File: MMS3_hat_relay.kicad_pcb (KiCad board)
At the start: 2 copper layers, 100 x 50 mm, 85 parts, among them J1 Chainbus in, J10 Conn_01x03_Pin, J2 Chainbus Out, J3 Conn_01x04_Pin, J5 Program, J6 Conn_01x03_Pin, J7 Conn_01x03_Pin, J8 Conn_01x03_Pin, J9 Conn_01x03_Pin, Q12 MMBT5551 200-300, Q13 MMBT5551 200-300, Q14 MMBT5551 200-300, Q15 MMBT5551 200-300, Q16 MMBT5551 200-300, U1 SN74CB3Q3384APW, U2 M24C64, U3 CH32V003FxPx, U4 AMS1117, U5 LTV-217-B-G, U6 LTV-217-B-G, U7 LTV-217-B-G, U8 LTV-217-B-G, U9 LTV-217-B-G, X1 X322525MOB4SI

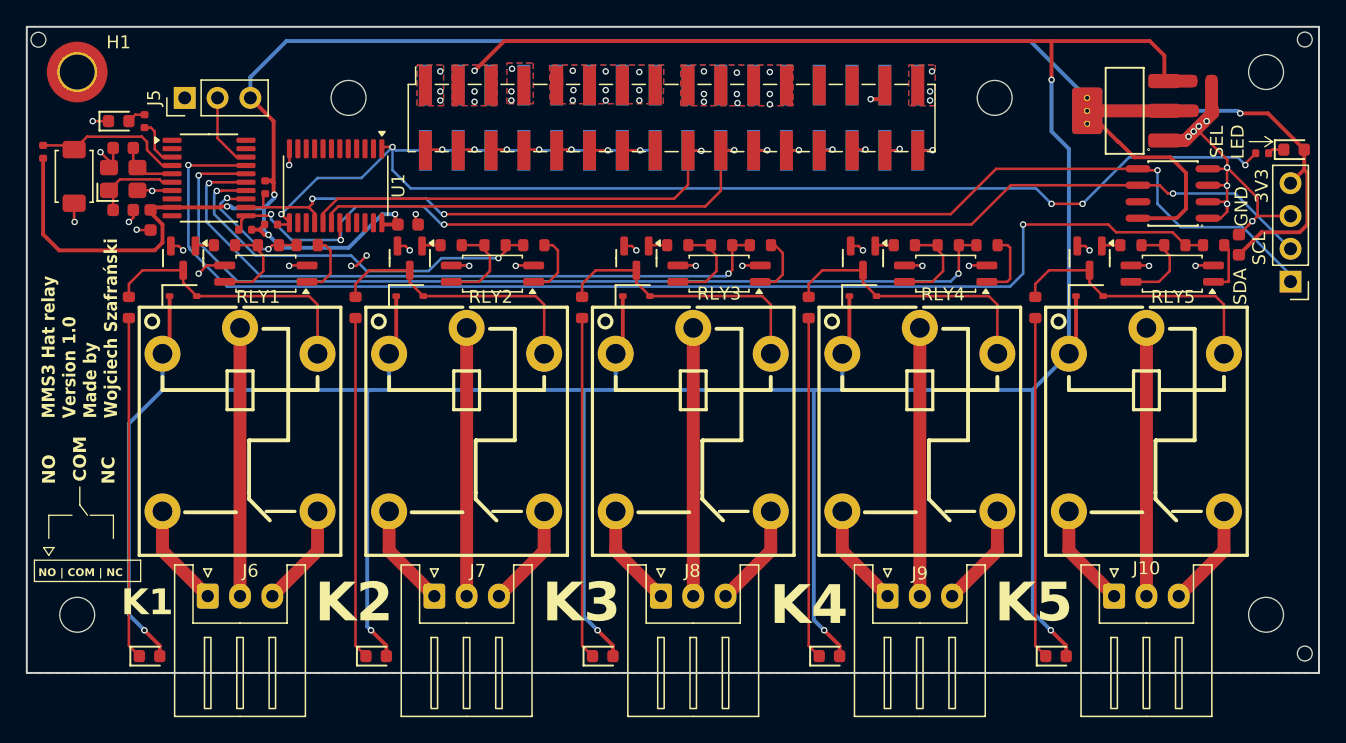
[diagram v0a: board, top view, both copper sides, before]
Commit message: fixed NPN configuration in optocoupler
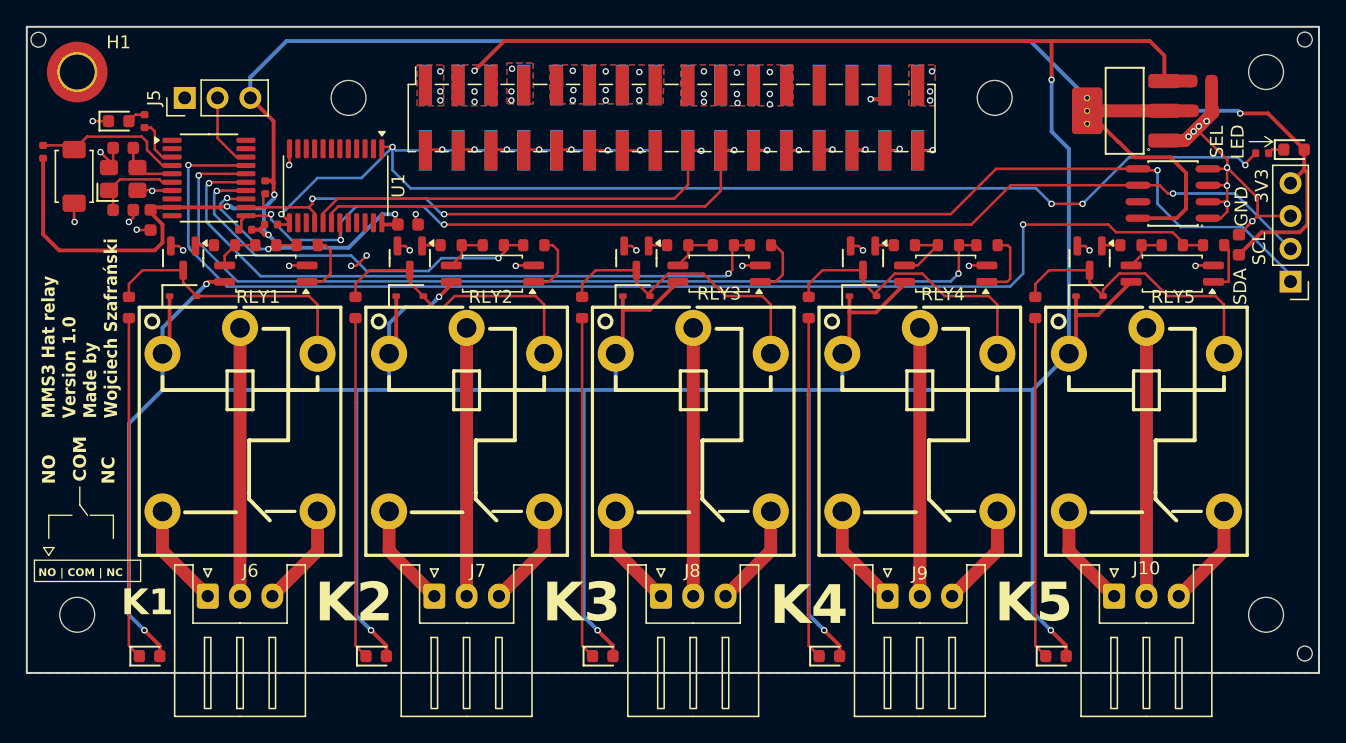
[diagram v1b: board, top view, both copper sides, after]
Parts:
- moved R15 0.20 mm to (96.6, 105.4)
- moved R28 0.20 mm to (166.7, 105.4)
- moved R19 0.14 mm to (114.2, 105.4)
- moved R22 0.13 mm to (132.0, 105.4)
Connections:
- U5 pad 3: GND -> Net-(R15-Pad2)
- U5 pad 4: Net-(R15-Pad2) -> +5V
- U6 pad 3: GND -> Net-(R19-Pad2)
- U6 pad 4: Net-(R19-Pad2) -> +5V
- U7 pad 3: GND -> Net-(R22-Pad2)
- U7 pad 4: Net-(R22-Pad2) -> +5V
- U8 pad 3: GND -> Net-(R25-Pad2)
- U8 pad 4: Net-(R25-Pad2) -> +5V
- U9 pad 3: GND -> Net-(R28-Pad2)
- U9 pad 4: Net-(R28-Pad2) -> +5V
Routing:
- net +5V: track 298.1 -> 331.3 mm, vias 9 -> 11
- net GND: track 66.2 -> 58.3 mm, vias 51 -> 46
- net Net-(R28-Pad2): track 7.04 -> 3.46 mm
- net Net-(R15-Pad2): track 7.04 -> 3.46 mm
- net Net-(R19-Pad2): track 7.04 -> 3.52 mm
- net Net-(R22-Pad2): track 7.04 -> 3.79 mm
- net Net-(R25-Pad2): track 7.04 -> 5.00 mm
- net Net-(Q16-C): track 21.5 -> 23.2 mm
- net Net-(Q15-C): track 21.5 -> 23.1 mm
- net Net-(Q14-C): track 21.5 -> 23.1 mm
- net Net-(Q13-C): track 21.5 -> 22.2 mm

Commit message: changed headers and relays to better one
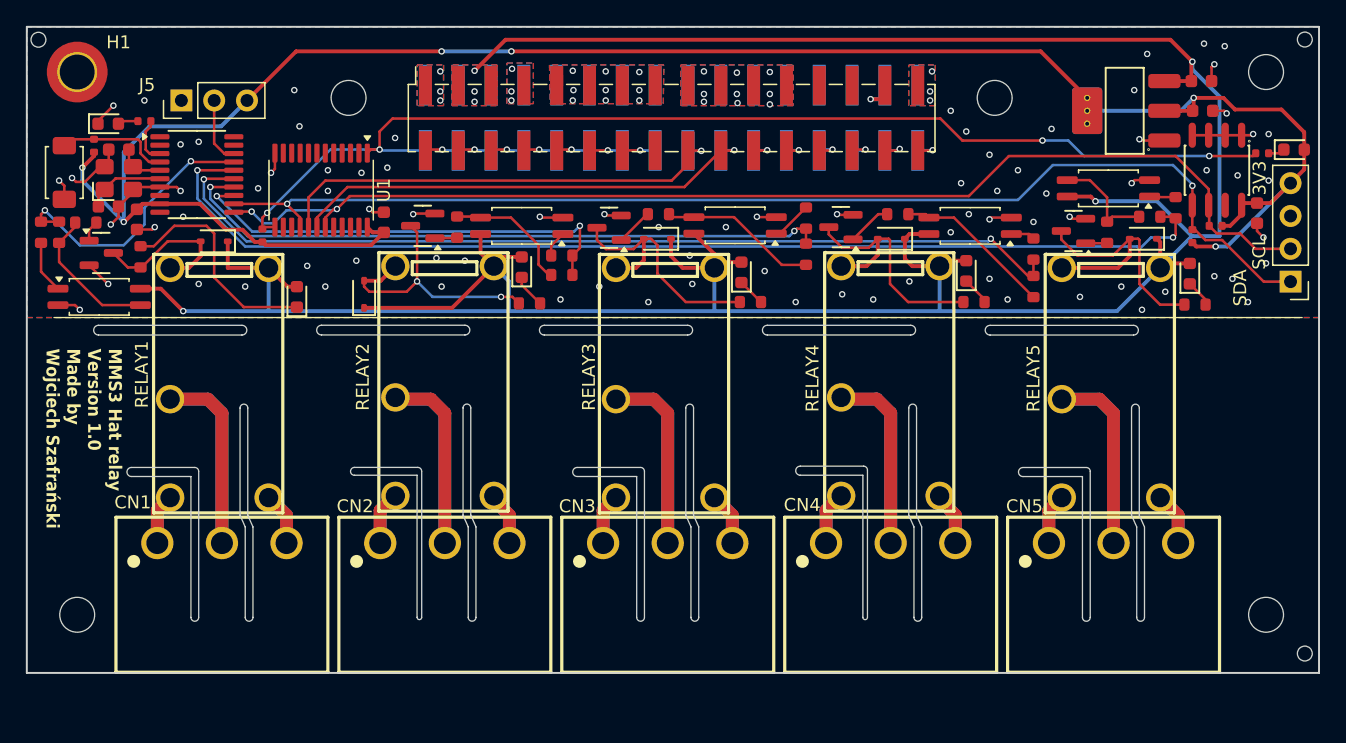
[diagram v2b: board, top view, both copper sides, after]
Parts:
- removed J10, J6, J7, J8, J9: Conn_01x03_Pin, Connector_JST:JST_XH_S3B-XH-A_1x03_P2.50mm_Horizontal
- removed RLY1, RLY2, RLY3, RLY4, RLY5: SRD-05VDC-SL-C, SRD-05VDC-SL-C:RELAY-TH_SRD-XXVDC-XL-C
- added CN1: DB2ERC-5.0-3P-GN, DB2ERC-5:CONN-TH_3P-P5.00_DB2ERC-5.0-3P-GN, F.Cu at (93.2, 128.4)
- added CN2: DB2ERC-5.0-3P-GN, DB2ERC-5:CONN-TH_3P-P5.00_DB2ERC-5.0-3P-GN, F.Cu at (110.5, 128.4)
- added CN3: DB2ERC-5.0-3P-GN, DB2ERC-5:CONN-TH_3P-P5.00_DB2ERC-5.0-3P-GN, F.Cu at (127.7, 128.4)
- added CN4: DB2ERC-5.0-3P-GN, DB2ERC-5:CONN-TH_3P-P5.00_DB2ERC-5.0-3P-GN, F.Cu at (144.9, 128.4)
- added CN5: DB2ERC-5.0-3P-GN, DB2ERC-5:CONN-TH_3P-P5.00_DB2ERC-5.0-3P-GN, F.Cu at (162.2, 128.4)
- added RELAY1: JE-105D_C3250129, JE-105D_C3250129:RELAY-TH_JE-1XXD, F.Cu at (93.0, 116.0)
- added RELAY2: JE-105D_C3250129, JE-105D_C3250129:RELAY-TH_JE-1XXD, F.Cu at (110.4, 115.9)
- added RELAY3: JE-105D_C3250129, JE-105D_C3250129:RELAY-TH_JE-1XXD, F.Cu at (127.5, 116.0)
- added RELAY4: JE-105D_C3250129, JE-105D_C3250129:RELAY-TH_JE-1XXD, F.Cu at (144.9, 115.9)
- added RELAY5: JE-105D_C3250129, JE-105D_C3250129:RELAY-TH_JE-1XXD, F.Cu at (162.0, 116.0)
- moved R6 75.1 mm to (170.1, 103.9)
- moved R10 71.8 mm to (168.3, 104.7), turned to 90 degrees
- moved D10 32.1 mm to (116.4, 107.1), turned to 90 degrees
- moved D12 31.6 mm to (150.8, 107.4), turned to 90 degrees
- moved D11 31.6 mm to (133.4, 107.5), turned to 90 degrees
- moved D13 31.4 mm to (168.1, 107.6), turned to 90 degrees
- moved D9 30.0 mm to (99.0, 109.4), turned to 90 degrees
- moved R17 20.6 mm to (79.2, 104.4), turned to -90 degrees
- moved R15 16.0 mm to (80.6, 104.4), turned to -90 degrees
- moved R31 13.5 mm to (117.0, 109.9), turned to 0 degrees
- moved R32 13.0 mm to (134.1, 109.8), turned to 0 degrees
- moved U5 13.0 mm to (83.7, 109.4), turned to 0 degrees
- moved R33 12.8 mm to (151.4, 109.8), turned to 0 degrees
- moved R34 12.4 mm to (168.5, 110.0), turned to 0 degrees
- moved R16 10.9 mm to (82.7, 103.7), turned to 0 degrees
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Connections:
- U3 pad 13: /S1 -> /S2
- U3 pad 14: /S2 -> /S3
- U3 pad 15: /S3 -> /S4
- U3 pad 16: /S4 -> /S5
- U3 pad 17: /S5 -> /S1
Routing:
- net +5V: track 331.3 -> 235.9 mm, vias 11 -> 6
- net Net-(D13-Pad1): track 26.5 -> 2.12 mm
- net Net-(D11-Pad1): track 26.5 -> 2.15 mm
- net Net-(D12-Pad1): track 26.5 -> 2.21 mm
- net Net-(D10-Pad1): track 26.5 -> 2.60 mm
- net +3V3: track 181.2 -> 158.4 mm, vias 5 -> 6
- net GND: track 58.3 -> 46.4 mm, vias 46 -> 102
- net /S1: track 9.87 -> 21.6 mm
- net /S5: track 95.5 -> 85.3 mm
- net Net-(Q12-C): track 21.5 -> 12.0 mm
- net Net-(D9-Pad1): track 26.5 -> 17.4 mm
- net Net-(R22-Pad2): track 3.79 -> 12.2 mm
- net /Relay 3/COM: track 20.8 -> 29.0 mm
- net /Relay 2/COM: track 20.8 -> 29.0 mm
- net /Relay 1/COM: track 20.8 -> 29.0 mm
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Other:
- outline, holes or cut-outs redrawn
- board text added: "+11mm"
- board text added: "+13.5"
- board text added: "+14mm"
- board text added: "2.5mm"
- board text added: "2mm"
- board text added: "5mm"
- board text added: "J1"
- board text added: "for 400V (230VAC) Clearance: 5.5mm (We use ~5mm due to headers Creepage: 15.75mm"
- board text added: "{ "ViaStitching": "0.2", "Bottom_Pour": { "HSpacing": "1", "VSpacing": "1", "HOffset": ".2", "VOffset": "0", "Clearance": ".2", "Randomize": true } }"
- board text added: "{ "ViaStitching": "0.2", "Bottom_Pour": { "HSpacing": "1", "VSpacing": "1", "HOffset": "0", "VOffset": "0", "Clearance": ".2", "Randomize": false } }"
- board text added: "{ "ViaStitching": "0.2", "Bottom_Pour": { "HSpacing": "5", "VSpacing": "5", "HOffset": "0", "VOffset": "0", "Clearance": ".2", "Randomize": false } }"
- board text removed: "GND"
- board text removed: "NO | COM | NC"
- board text removed: "SEL LED"

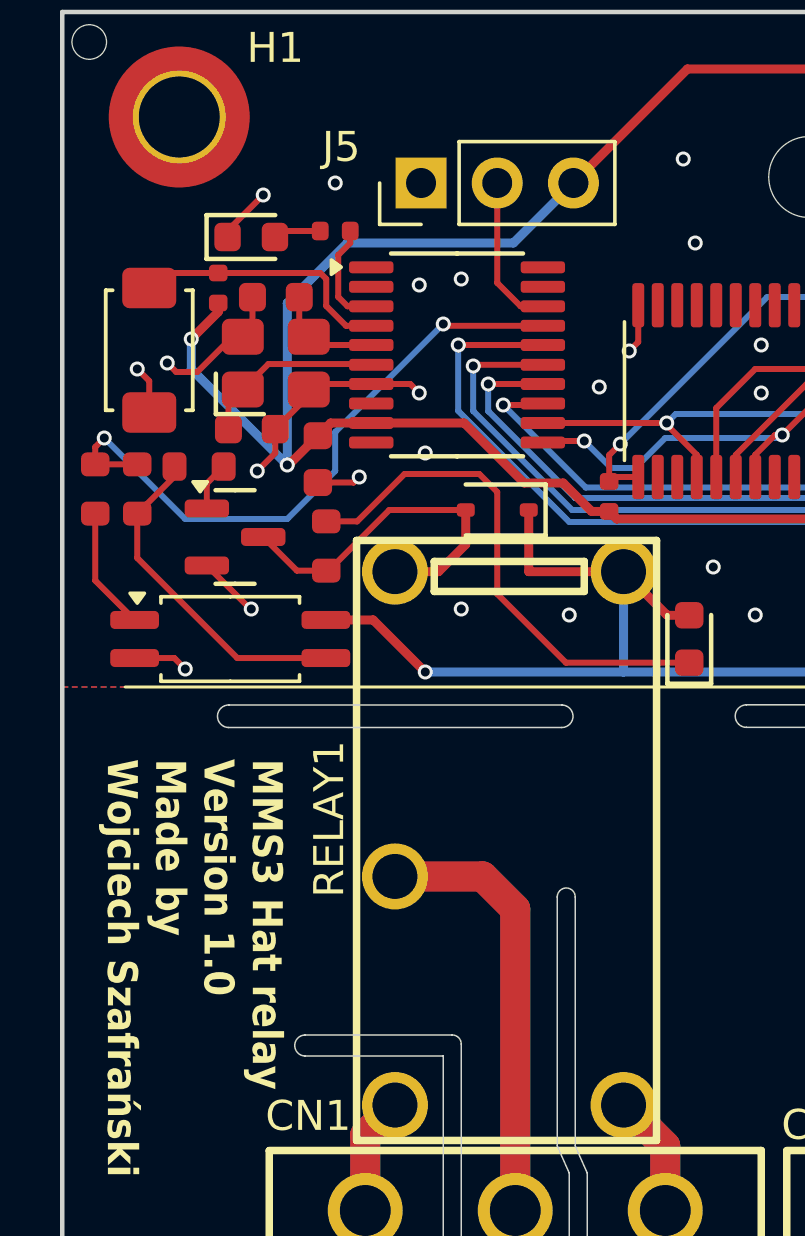
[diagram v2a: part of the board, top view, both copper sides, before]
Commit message: BREAKING: updated CH32v003 programming pinout
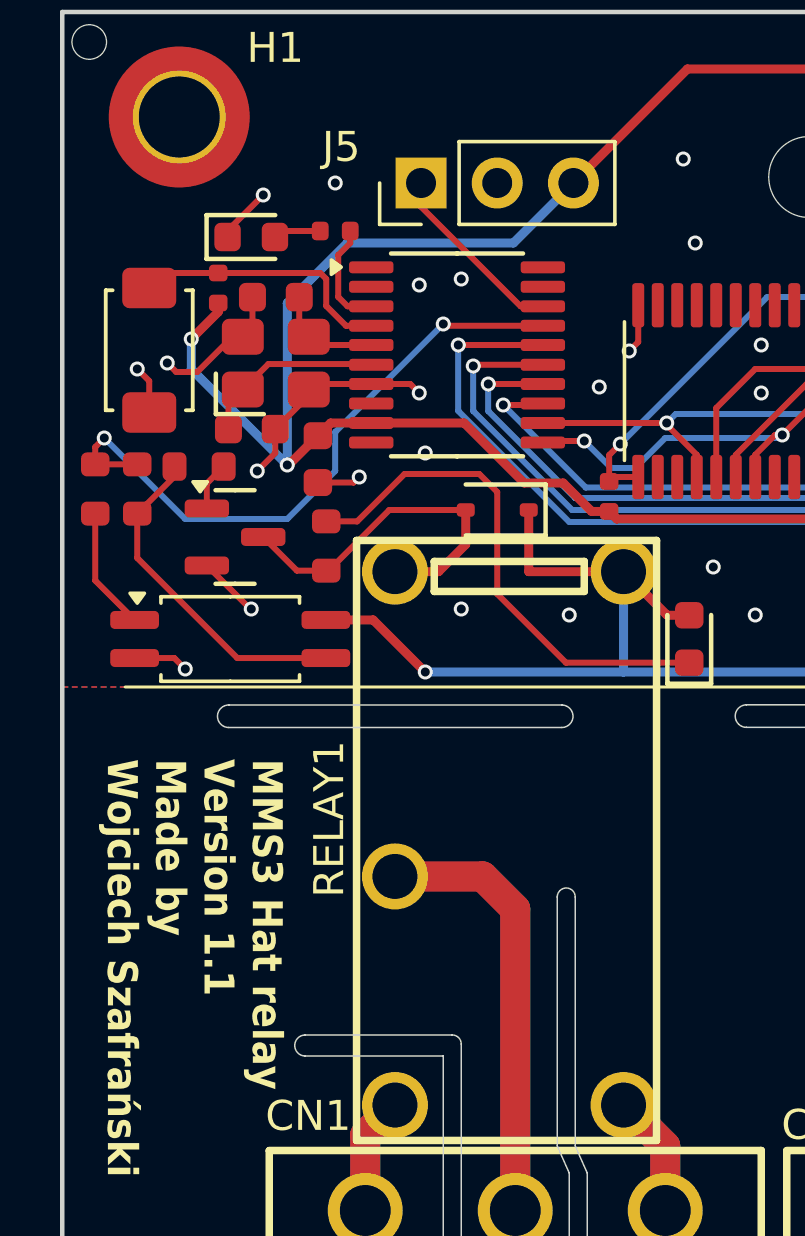
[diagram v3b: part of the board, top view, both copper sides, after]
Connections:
- J5 pad 1: GND -> /CH32V003/SWIO
- J5 pad 2: /CH32V003/SWIO -> GND
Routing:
- net /CH32V003/SWIO: track 5.17 -> 6.23 mm
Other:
- board text added: "MMS3 Hat relay Version 1.1 Made by Wojciech Szafrański"
- board text removed: "MMS3 Hat relay Version 1.0 Made by Wojciech Szafrański"
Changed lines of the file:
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@@
 	(title_block
 		(title "MMS3 Hat Relay")
-		(date "2137-02-25")
-		(rev "R0")
+		(date "2026-06-08")
+		(rev "1.1")
 		(comment 1 "Made by Wojciech Szafrański")
 		(comment 2 "Designed in poland")
@@
 			(layers "*.Cu" "*.Mask")
 			(remove_unused_layers no)
-			(net "GND")
+			(net "/CH32V003/SWIO")
 			(pinfunction "Pin_1_1")
 			(pintype "passive")
@@
 			(layers "*.Cu" "*.Mask")
 			(remove_unused_layers no)
-			(net "/CH32V003/SWIO")
+			(net "GND")
 			(pinfunction "Pin_2_2")
 			(pintype "passive")
@@
 		(layer "User.4")
 	)
-	(gr_text "MMS3 Hat relay\nVersion 1.0\nMade by \nWojciech Szafrański"
+	(gr_text "MMS3 Hat relay\nVersion 1.1\nMade by \nWojciech Szafrański"
 		(at 82.5 113.4 270)
 		(layer "F.SilkS")
@@
 	)
 	(segment
-		(start 92.6 97.529999)
+		(start 90.06 94.989999)
 		(end 93.380001 98.31)
 		(width 0.2)
@@
 	)
 	(segment
-		(start 92.6 94.2)
-		(end 92.6 97.529999)
+		(start 90.06 94.2)
+		(end 90.06 94.989999)
 		(width 0.2)
 		(layer "F.Cu")
